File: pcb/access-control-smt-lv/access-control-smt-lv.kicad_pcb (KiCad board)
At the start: 2 copper layers, 65.9 x 33.8 mm, 30 parts, among them U1 ESP32-WROOM-E

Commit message: SMT PCB Updates
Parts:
- added CON_5v2: Conn_01x02_Socket, Connector_PinHeader_2.54mm:PinHeader_1x02_P2.54mm_Vertical, F.Cu at (47.5, 31.9)
- added R_PRGM_SERIAL1: 10kR, Resistor_SMD:R_1206_3216Metric_Pad1.30x1.75mm_HandSolder, F.Cu at (42.8, 22.2)
- C1: footprint Capacitor_SMD:C_1808_4520Metric_Pad1.72x2.30mm_HandSolder -> Capacitor_SMD:C_1206_3216Metric_Pad1.33x1.80mm_HandSolder
- moved C3 1.09 mm to (47.5, 27.6)
- moved C_PWR_3v3 1.09 mm to (44.4, 27.6)
- moved C1 0.23 mm to (12.2, 3.85)
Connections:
- U1 pad 24: unconnected-(U1-ADC2_CH2/GPIO2-Pad24) -> Net-(U1-ADC2_CH2/GPIO2)
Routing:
- net GND: track 295.4 -> 306.6 mm
- net +5V: track 81.1 -> 85.2 mm, vias 2 -> 3
- net Net-(U1-ADC2_CH2/GPIO2): track 0.00 -> 3.17 mm
- net Net-(J_BUTTON1-Pin_1): track 52.2 -> 50.9 mm

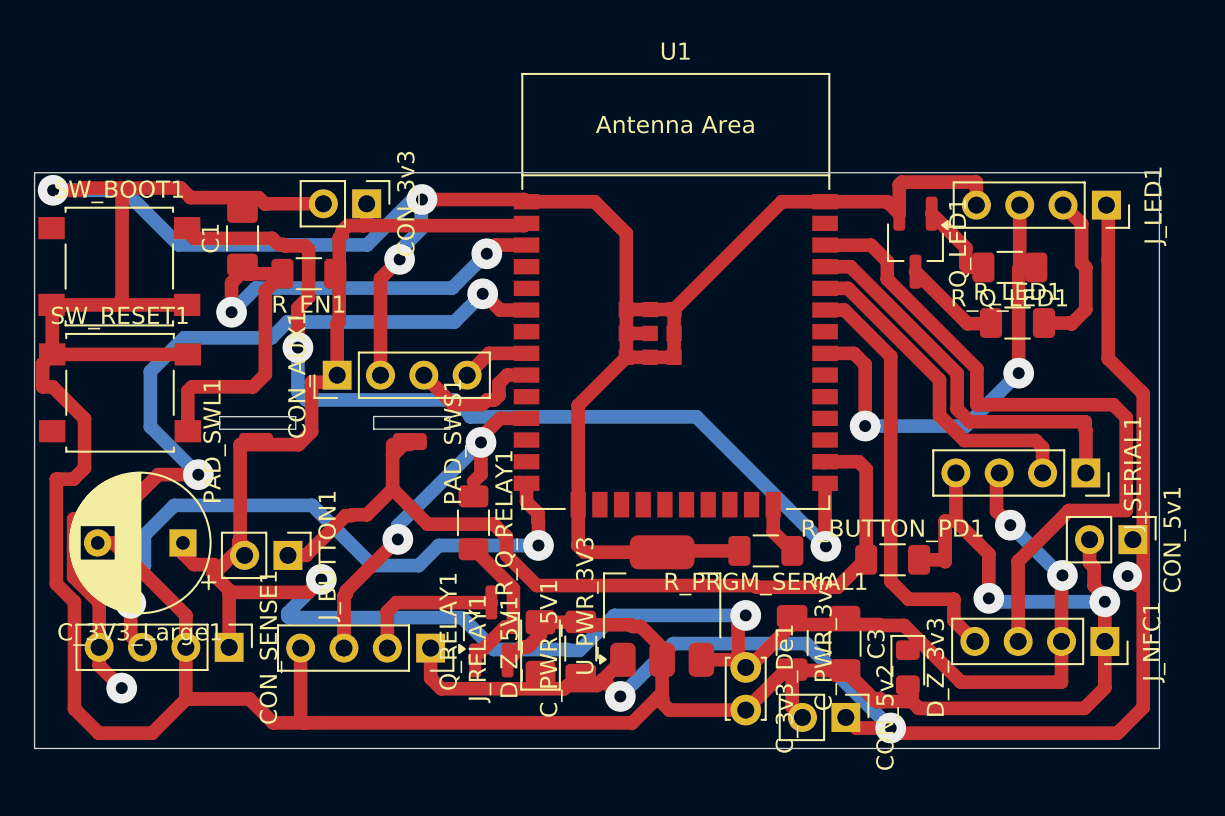
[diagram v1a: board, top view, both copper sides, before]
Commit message: Fixes to relief, JST connectors for SMT board
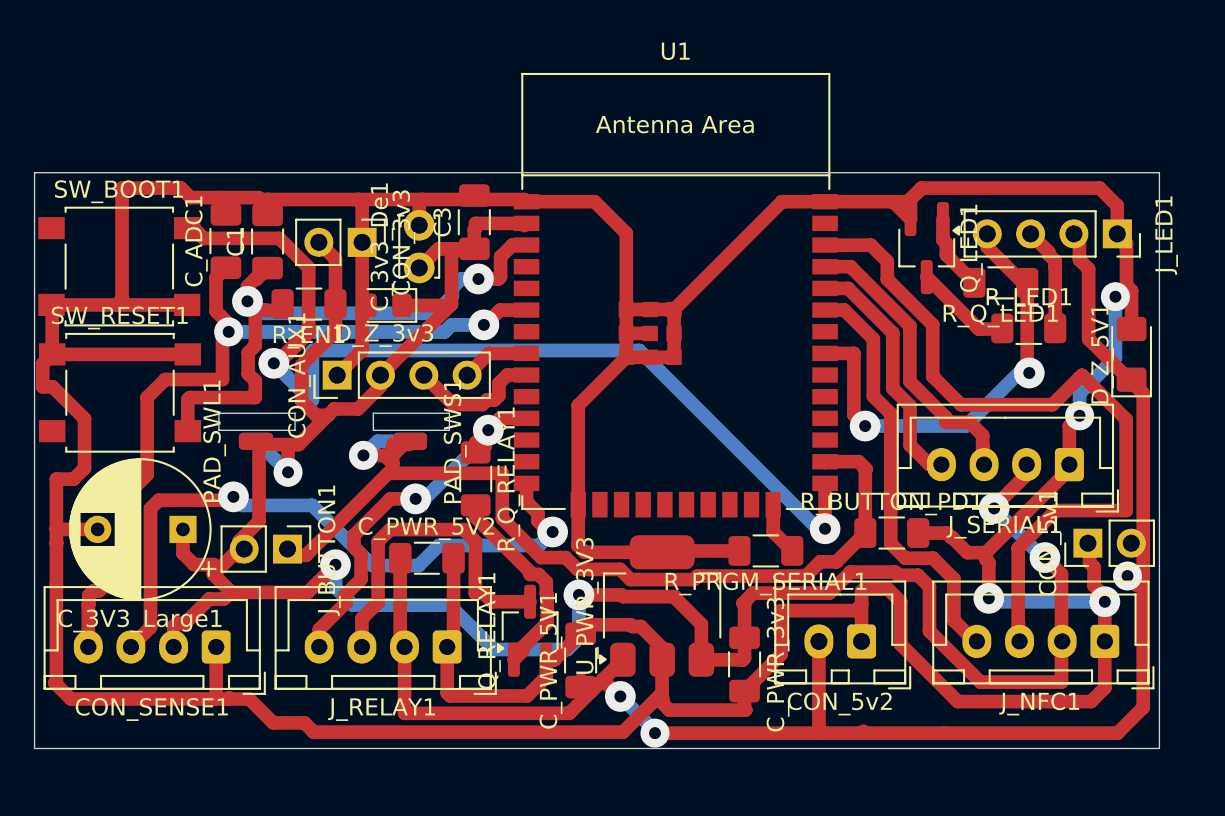
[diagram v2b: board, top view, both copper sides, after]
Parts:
- added C_ADC1: 100N, Capacitor_SMD:C_1206_3216Metric_Pad1.33x1.80mm_HandSolder, F.Cu at (11.2, 4.02)
- added C_PWR_5V2: 0.1U, Capacitor_SMD:C_1206_3216Metric_Pad1.33x1.80mm_HandSolder, F.Cu at (23.0, 22.6)
- added PAD_SWL2: Conn_01x01_Female, Connector_Wire:SolderWirePad_1x01_SMD_1x2mm, B.Cu at (12.9, 15.8)
- added PAD_SWS2: Conn_01x01_Female, Connector_Wire:SolderWirePad_1x01_SMD_1x2mm, B.Cu at (22.0, 15.8)
- CON_5v2: footprint Connector_PinHeader_2.54mm:PinHeader_1x02_P2.54mm_Vertical -> Connector_JST:JST_XH_B2B-XH-A_1x02_P2.50mm_Vertical
- CON_SENSE1: footprint Connector_PinHeader_2.54mm:PinHeader_1x04_P2.54mm_Vertical -> Connector_JST:JST_XH_B4B-XH-A_1x04_P2.50mm_Vertical
- J_NFC1, J_RELAY1, J_SERIAL1: footprint Connector_PinSocket_2.54mm:PinSocket_1x04_P2.54mm_Vertical -> Connector_JST:JST_XH_B4B-XH-A_1x04_P2.50mm_Vertical
- moved D_Z_5V1 38.7 mm to (64.3, 10.7)
- moved D_Z_3v3 37.3 mm to (20.5, 7.79), turned to 180 degrees
- moved C3 32.9 mm to (25.8, 2.91), turned to 90 degrees
- moved C_3v3_De1 30.2 mm to (22.5, 5.59), turned to 90 degrees
- moved CON_5v2 4.55 mm to (48.5, 27.5), turned to 180 degrees
- moved C_PWR_3v3 3.06 mm to (41.6, 28.8)
- moved CON_5v1 2.64 mm to (61.7, 21.7), turned to 90 degrees
- moved R_Q_RELAY1 2.57 mm to (25.8, 18.0)
- moved CON_3v3 2.28 mm to (19.2, 4.09)
- moved Q_RELAY1 2.27 mm to (29.0, 26.9)
- moved J_LED1 1.80 mm to (63.4, 3.60)
- moved R_EN1 1.78 mm to (16.1, 7.71)
- moved R_BUTTON_PD1 1.57 mm to (50.2, 21.1)
- moved C1 1.48 mm to (13.6, 4.04)
- moved J_SERIAL1 1.09 mm to (60.6, 17.1), turned to 180 degrees
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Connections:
- CON_3v3 pad 1: +3V3 -> GND
- CON_3v3 pad 2: GND -> +3V3
- CON_5v1 pad 1: +5V -> GND
- CON_5v1 pad 2: GND -> +5V
- CON_5v2 pad 1: +5V -> GND
- CON_5v2 pad 2: GND -> +5V
- CON_AUX1 pad 1: +3V3 -> GND
- CON_AUX1 pad 2: GND -> +3V3
- CON_SENSE1 pad 1: +3V3 -> GND
- CON_SENSE1 pad 2: GND -> +3V3
- J_LED1 pad 1: +5V -> GND
- J_LED1 pad 2: Net-(J_LED1-Pin_2) -> +5V
- J_LED1 pad 4: GND -> Net-(J_LED1-Pin_4)
- J_RELAY1 pad 1: +5V -> GND
- J_RELAY1 pad 2: Net-(J_RELAY1-Pin_2) -> +5V
- J_RELAY1 pad 4: GND -> Net-(J_RELAY1-Pin_4)
- J_SERIAL1 pad 1: Net-(J_SERIAL1-Pin_1) -> GND
- J_SERIAL1 pad 2: Net-(J_SERIAL1-Pin_2) -> +3V3
- J_SERIAL1 pad 3: +3V3 -> Net-(J_SERIAL1-Pin_3)
- J_SERIAL1 pad 4: GND -> Net-(J_SERIAL1-Pin_4)
- Q_RELAY1 pad 3: Net-(J_RELAY1-Pin_2) -> Net-(J_RELAY1-Pin_3)
- R_LED1 pad 2: Net-(J_LED1-Pin_2) -> Net-(J_LED1-Pin_3)
- R_Q_LED1 pad 1: Net-(J_LED1-Pin_3) -> Net-(J_LED1-Pin_4)
- R_Q_RELAY1 pad 1: Net-(J_RELAY1-Pin_3) -> Net-(J_RELAY1-Pin_4)
- U1 pad 11: Net-(J_RELAY1-Pin_3) -> Net-(J_RELAY1-Pin_4)
- U1 pad 31: Net-(J_LED1-Pin_3) -> Net-(J_LED1-Pin_4)
- U1 pad 34: Net-(J_SERIAL1-Pin_2) -> Net-(J_SERIAL1-Pin_4)
- U1 pad 35: Net-(J_SERIAL1-Pin_1) -> Net-(J_SERIAL1-Pin_3)
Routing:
- net Net-(J_LED1-Pin_4): track 0.00 -> 26.5 mm, vias 0 -> 2
- net +3V3: track 125.8 -> 150.9 mm, vias 4 -> 5
- net Net-(J_RELAY1-Pin_4): track 0.00 -> 23.7 mm, vias 0 -> 2
- net Net-(J_SERIAL1-Pin_1): track 23.3 -> 0.00 mm
- net Net-(J_LED1-Pin_3): track 27.4 -> 6.14 mm, vias 2 -> 0
- net Net-(J_SERIAL1-Pin_2): track 19.3 -> 0.00 mm
- net Net-(J_SERIAL1-Pin_3): track 0.00 -> 18.3 mm
- net GND: track 306.6 -> 324.5 mm, vias 5 -> 4
- net Net-(J_SERIAL1-Pin_4): track 0.00 -> 14.4 mm
- net +5V: track 85.2 -> 94.8 mm
- net Net-(J_LED1-Pin_2): track 9.50 -> 0.00 mm
- net Net-(J_RELAY1-Pin_2): track 8.45 -> 0.00 mm
- net Net-(CON_SENSE1-Pin_4): track 51.0 -> 46.3 mm, vias 3 -> 2
- net Net-(J_BUTTON1-Pin_1): track 50.9 -> 55.5 mm, vias 0 -> 1
- net Net-(U1-GPIO0/BOOT/ADC2_CH1): track 55.7 -> 59.1 mm
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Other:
- outline, holes or cut-outs redrawn
